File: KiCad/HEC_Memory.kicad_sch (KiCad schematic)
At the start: 11 parts, among them U10 74LS32, U13 74LS245, U14 74LS245, U15 74LS32, U16 74LS32, U2 AS6C4008-55PCN, U22 74LS02, U3 AS6C4008-55PCN, U4 CY7C199, U5 CY7C199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

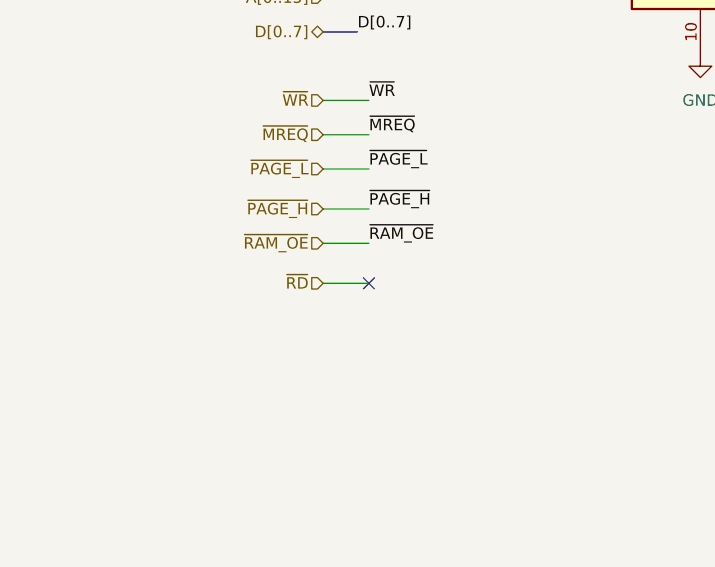
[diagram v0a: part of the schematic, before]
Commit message: Removed DMA from bus
Bus-mastering DMA has been removed from the expansion bus design due to complexity and bandwidth issue with external bus expansion circuit. The pins are replaced with audio output from on-bard sound system. Minor changes to pin names.
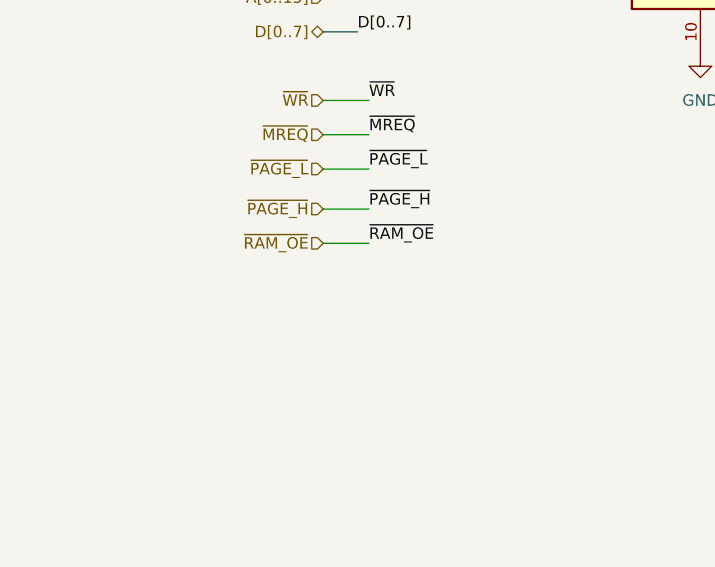
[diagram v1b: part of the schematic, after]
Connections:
- no-connect marks 2 -> 1
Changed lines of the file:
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@@
   (junction (at 104.14 87.63) (diameter 0) (color 0 0 0 0)
   )
-  (no_connect (at 52.07 86.36))
   (no_connect (at 143.51 172.72))
   (wire (pts (xy 269.24 45.72) (xy 271.78 45.72))
@@
   )
   (wire (pts (xy 182.88 71.12) (xy 185.42 71.12))
-    (stroke (width 0) (type default))
-  )
-  (wire (pts (xy 46.99 86.36) (xy 52.07 86.36))
     (stroke (width 0) (type default))
   )
@@
     (effects (font (size 1.27 1.27)) (justify right))
   )
-  (hierarchical_label "~{RD}" (shape input) (at 46.99 86.36 180) (fields_autoplaced)
-    (effects (font (size 1.27 1.27)) (justify right))
-  )

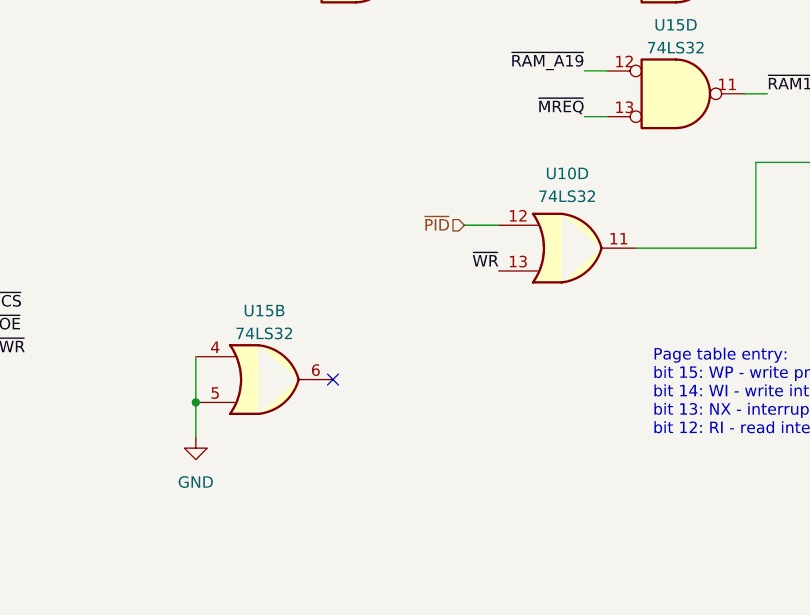
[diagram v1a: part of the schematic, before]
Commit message: Preliminary layout
Very early stage layout prototype, very subject to change.
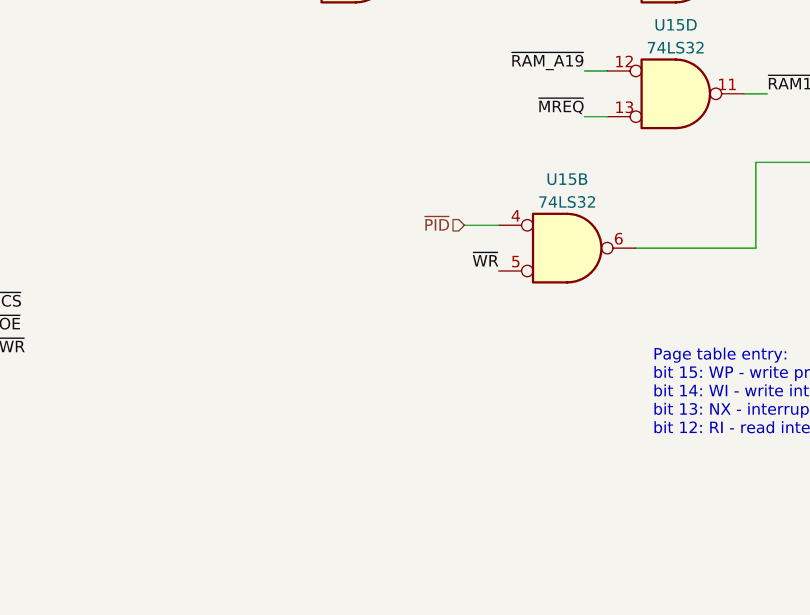
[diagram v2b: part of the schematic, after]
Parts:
- removed U10: 74LS32, Package_DIP:DIP-14_W7.62mm_Socket, symbol 74xx:74LS32
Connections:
- net GND: no longer U15.4, U15.5
- net ~{PID}: now also U15.4
- net ~{WR}: now also U15.5
- net at U15.6: now also U9.11 (Cp)
- no-connect marks 1 -> 0
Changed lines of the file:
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@@
 (kicad_sch (version 20230121) (generator eeschema)
   (paper "A4")
-  (junction (at 128.27 175.26) (diameter 0) (color 0 0 0 0)
-  )
   (junction (at 104.14 87.63) (diameter 0) (color 0 0 0 0)
   )
-  (no_connect (at 143.51 172.72))
   (wire (pts (xy 269.24 45.72) (xy 271.78 45.72))
     (stroke (width 0) (type default))
@@
     (stroke (width 0) (type default))
   )
-  (wire (pts (xy 128.27 170.18) (xy 128.27 175.26))
-    (stroke (width 0) (type default))
-  )
   (wire (pts (xy 22.86 167.64) (xy 25.4 167.64))
     (stroke (width 0) (type default))
@@
   )
   (wire (pts (xy 101.6 27.94) (xy 104.14 27.94))
-    (stroke (width 0) (type default))
-  )
-  (wire (pts (xy 128.27 175.26) (xy 128.27 179.07))
     (stroke (width 0) (type default))
   )
@@
         (path "/87935374-b60a-4f41-99da-94b76103dd77/933a6f90-eb98-4eb1-8c19-8a76228aece1"
           (reference "#PWR011") (unit 1)
-        )
-      )
-    )
-  )
-  (symbol (lib_id "power:GND") (at 128.27 179.07 0) (unit 1)
-    (in_bom yes) (on_board yes) (dnp no) (fields_autoplaced)
-    (property "Reference" "#PWR0108" (at 128.27 185.42 0)
-      (effects (font (size 1.27 1.27)) hide)
-    )
-    (property "Value" "GND" (at 128.27 184.15 0)
-      (effects (font (size 1.27 1.27)))
-    )
-    (property "Footprint" "" (at 128.27 179.07 0)
-      (effects (font (size 1.27 1.27)) hide)
-    )
-    (property "Datasheet" "" (at 128.27 179.07 0)
-      (effects (font (size 1.27 1.27)) hide)
-    )
-    (pin "1")
-    (instances
-      (project "HEC1"
-        (path "/87935374-b60a-4f41-99da-94b76103dd77"
-          (reference "#PWR0108") (unit 1)
-        )
-        (path "/87935374-b60a-4f41-99da-94b76103dd77/933a6f90-eb98-4eb1-8c19-8a76228aece1"
-          (reference "#PWR0109") (unit 1)
         )
       )
@@
     )
   )
-  (symbol (lib_id "74xx:74LS32") (at 135.89 172.72 0) (unit 2)
-    (in_bom yes) (on_board yes) (dnp no) (fields_autoplaced)
-    (property "Reference" "U15" (at 135.89 165.1 0)
-      (effects (font (size 1.27 1.27)))
-    )
-    (property "Value" "74LS32" (at 135.89 167.64 0)
-      (effects (font (size 1.27 1.27)))
-    )
-    (property "Footprint" "Package_DIP:DIP-14_W7.62mm_Socket" (at 135.89 172.72 0)
-      (effects (font (size 1.27 1.27)) hide)
-    )
-    (property "Datasheet" "http://www.ti.com/lit/gpn/sn74LS32" (at 135.89 172.72 0)
+  (symbol (lib_id "74xx:74LS32") (at 169.545 158.115 0) (unit 2) (convert 2)
+    (in_bom yes) (on_board yes) (dnp no) (fields_autoplaced)
+    (property "Reference" "U15" (at 169.545 150.495 0)
+      (effects (font (size 1.27 1.27)))
+    )
+    (property "Value" "74LS32" (at 169.545 153.035 0)
+      (effects (font (size 1.27 1.27)))
+    )
+    (property "Footprint" "Package_DIP:DIP-14_W7.62mm_Socket" (at 169.545 158.115 0)
+      (effects (font (size 1.27 1.27)) hide)
+    )
+    (property "Datasheet" "http://www.ti.com/lit/gpn/sn74LS32" (at 169.545 158.115 0)
       (effects (font (size 1.27 1.27)) hide)
     )
@@
         )
       )
-    )
-  )
-  (symbol (lib_id "74xx:74LS32") (at 169.545 158.115 0) (unit 4)
-    (in_bom yes) (on_board yes) (dnp no) (fields_autoplaced)
-    (property "Reference" "U10" (at 169.545 149.86 0)
-      (effects (font (size 1.27 1.27)))
-    )
-    (property "Value" "74LS32" (at 169.545 152.4 0)
-      (effects (font (size 1.27 1.27)))
-    )
-    (property "Footprint" "Package_DIP:DIP-14_W7.62mm_Socket" (at 169.545 158.115 0)
-      (effects (font (size 1.27 1.27)) hide)
-    )
-    (property "Datasheet" "http://www.ti.com/lit/gpn/sn74LS32" (at 169.545 158.115 0)
-      (effects (font (size 1.27 1.27)) hide)
-    )
-    (pin "1")
-    (pin "2")
-    (pin "3")
-    (pin "4")
-    (pin "5")
-    (pin "6")
-    (pin "10")
-    (pin "8")
-    (pin "9")
-    (pin "11")
-    (pin "12")
-    (pin "13")
-    (pin "14")
-    (pin "7")
-    (instances
-      (project "HEC1"
-        (path "/87935374-b60a-4f41-99da-94b76103dd77/933a6f90-eb98-4eb1-8c19-8a76228aece1"
-          (reference "U10") (unit 4)
-        )
-      )

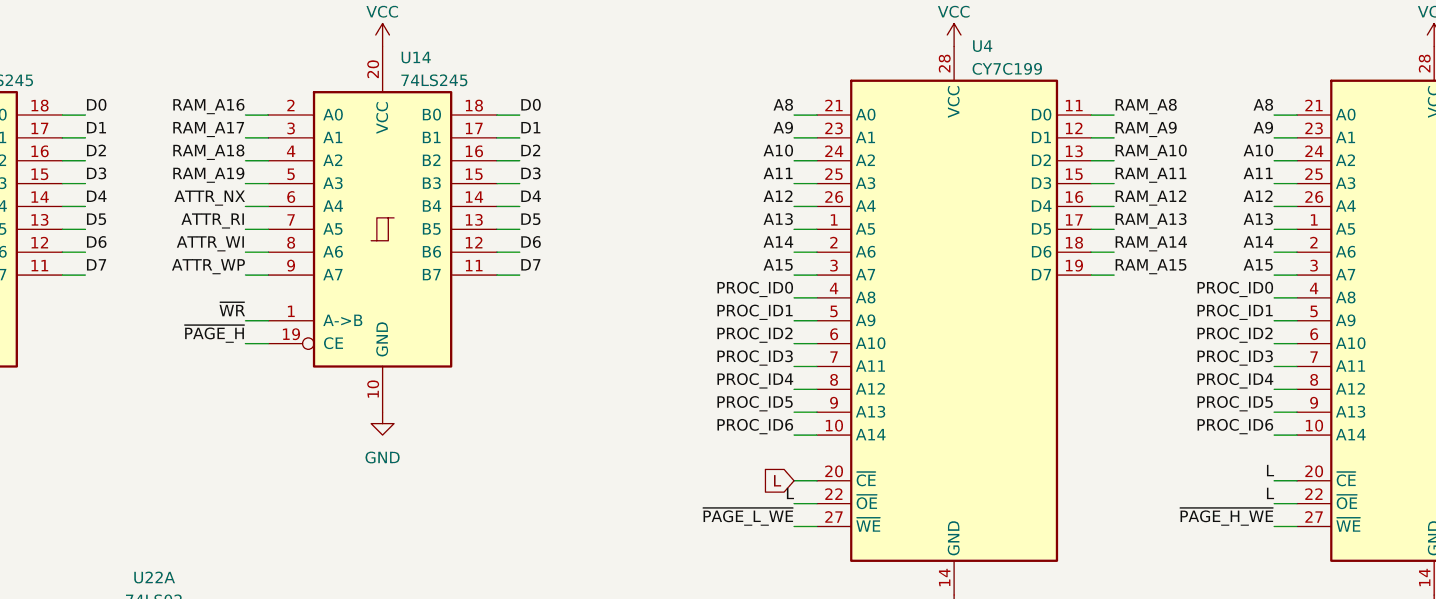
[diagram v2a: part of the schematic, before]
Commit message: Exchange RI and NX pins on bus driver
A mistake is found in the schematic: the RI and NX bits are exchanged on the 74245 bus driver chip. The mistake has been corrected. This change is significant since it changes the (non-existent) software programming model. More playing around with the layout.
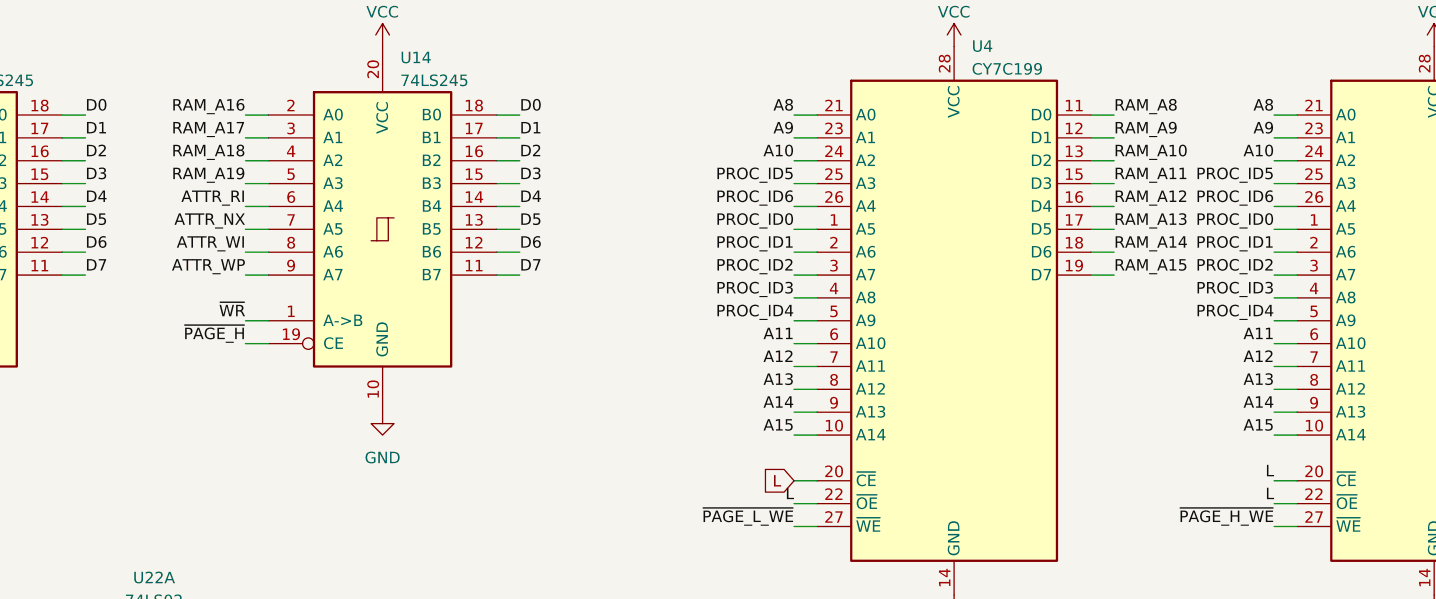
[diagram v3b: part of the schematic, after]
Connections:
- net A11: now also U4.6 (A10), U5.6 (A10); no longer U4.25 (A3), U5.25 (A3)
- net A12: now also U4.7 (A11), U5.7 (A11); no longer U4.26 (A4), U5.26 (A4)
- net A13: now also U4.8 (A12), U5.8 (A12); no longer U4.1 (A5), U5.1 (A5)
- net A14: now also U4.9 (A13), U5.9 (A13); no longer U4.2 (A6), U5.2 (A6)
- net A15: now also U4.10 (A14), U5.10 (A14); no longer U4.3 (A7), U5.3 (A7)
- net ATTR_NX: now also U14.7 (A5); no longer U14.6 (A4)
- net ATTR_RI: now also U14.6 (A4); no longer U14.7 (A5)
- net PROC_ID0: now also U4.1 (A5), U5.1 (A5); no longer U4.4 (A8), U5.4 (A8)
- net PROC_ID1: now also U4.2 (A6), U5.2 (A6); no longer U4.5 (A9), U5.5 (A9)
- net PROC_ID2: now also U4.3 (A7), U5.3 (A7); no longer U4.6 (A10), U5.6 (A10)
- net PROC_ID3: now also U4.4 (A8), U5.4 (A8); no longer U4.7 (A11), U5.7 (A11)
- net PROC_ID4: now also U4.5 (A9), U5.5 (A9); no longer U4.8 (A12), U5.8 (A12)
- net PROC_ID5: now also U4.25 (A3), U5.25 (A3); no longer U4.9 (A13), U5.9 (A13)
- net PROC_ID6: now also U4.26 (A4), U5.26 (A4); no longer U4.10 (A14), U5.10 (A14)
